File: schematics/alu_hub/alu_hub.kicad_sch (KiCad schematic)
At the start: 39 parts, among them U1 74LS574, U10 74LS02, U2 74LS245, U3 74LS02, U4 74LS181, U5 74LS181, U6 74LS574, U7 74LS245, U8 74LS245, U9 74LS02

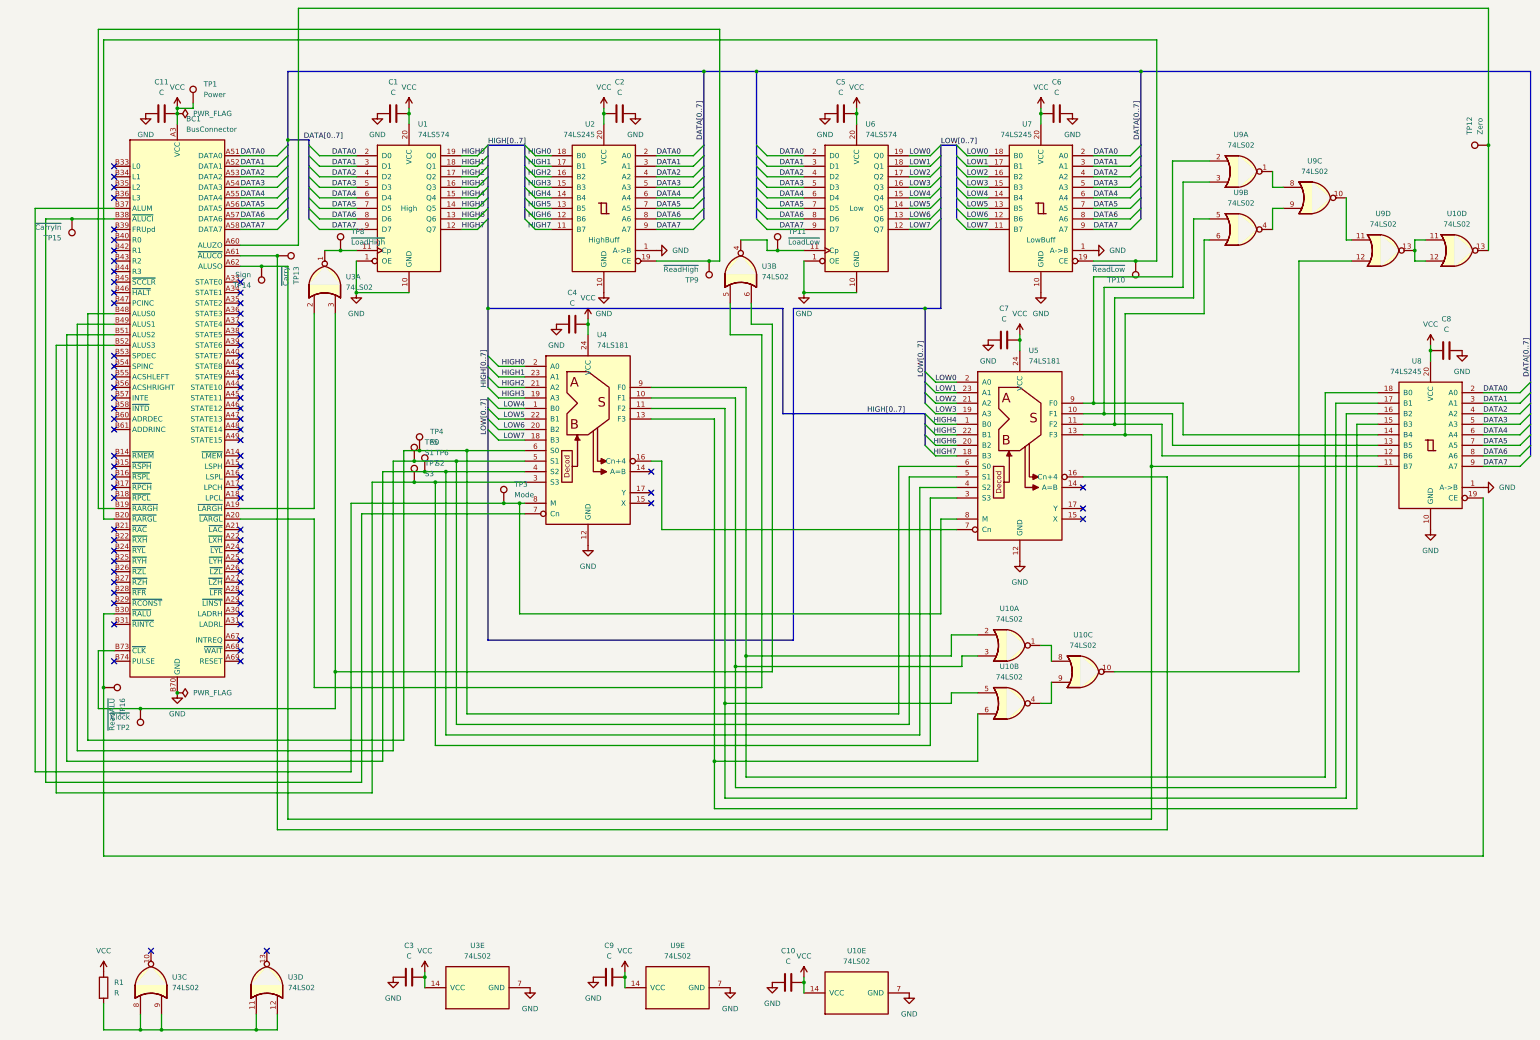
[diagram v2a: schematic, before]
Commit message: feat(alu): added tp to alu
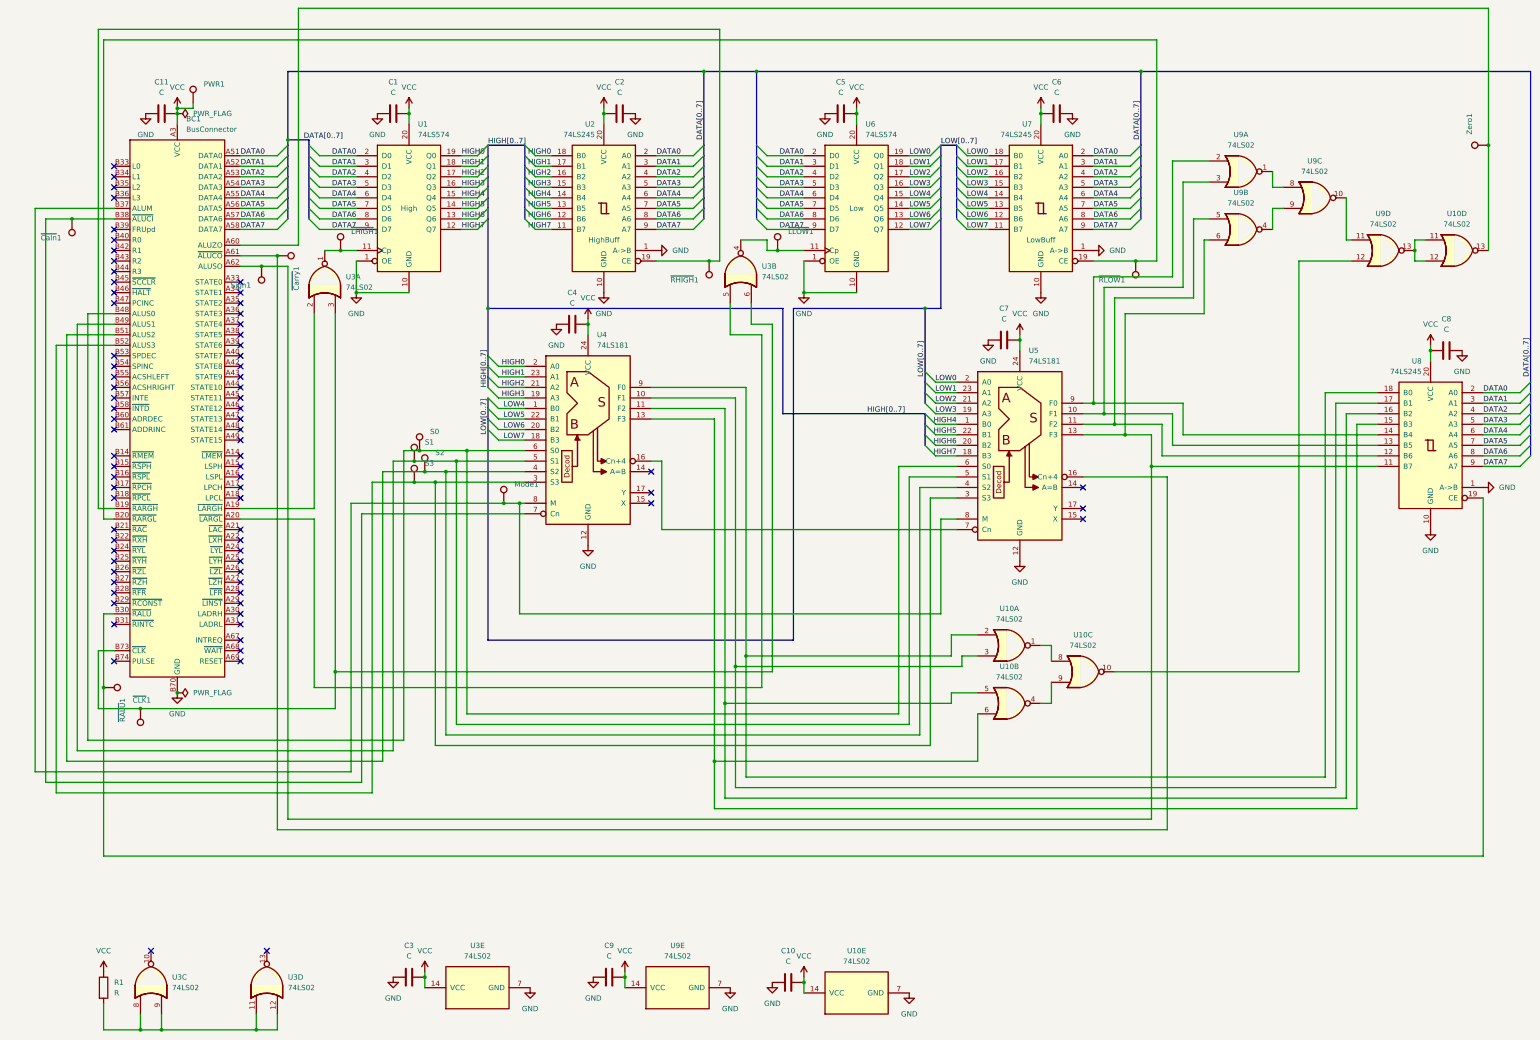
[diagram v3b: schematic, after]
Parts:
- Mode1: renamed from TP3; footprint Connector_Pin:Pin_D1.0mm_L10.0mm -> TestPoint:TestPoint_Pad_D1.0mm
- PWR1: renamed from TP1; footprint Connector_Pin:Pin_D1.0mm_L10.0mm -> TestPoint:TestPoint_Pad_D1.0mm
- S0: renamed from TP4; footprint Connector_Pin:Pin_D1.0mm_L10.0mm -> TestPoint:TestPoint_Pad_D1.0mm
- S1: renamed from TP5; footprint Connector_Pin:Pin_D1.0mm_L10.0mm -> TestPoint:TestPoint_Pad_D1.0mm
- S2: renamed from TP6; footprint Connector_Pin:Pin_D1.0mm_L10.0mm -> TestPoint:TestPoint_Pad_D1.0mm
- S3: renamed from TP7; footprint Connector_Pin:Pin_D1.0mm_L10.0mm -> TestPoint:TestPoint_Pad_D1.0mm
- Sign1: renamed from TP14; footprint Connector_Pin:Pin_D1.0mm_L10.0mm -> TestPoint:TestPoint_Pad_D1.0mm
- Zero1: renamed from TP12; footprint Connector_Pin:Pin_D1.0mm_L10.0mm -> TestPoint:TestPoint_Pad_D1.0mm
- ~{CLK}1: renamed from TP2; footprint Connector_Pin:Pin_D1.0mm_L10.0mm -> TestPoint:TestPoint_Pad_D1.0mm
- ~{CaIn}1: renamed from TP15; value ~{CarryIn} -> ~{CaIn}; footprint Connector_Pin:Pin_D1.0mm_L10.0mm -> TestPoint:TestPoint_Pad_D1.0mm
- ~{Carry}1: renamed from TP13; footprint Connector_Pin:Pin_D1.0mm_L10.0mm -> TestPoint:TestPoint_Pad_D1.0mm
- ~{LHIGH}1: renamed from TP8; footprint Connector_Pin:Pin_D1.0mm_L10.0mm -> TestPoint:TestPoint_Pad_D1.0mm
- ~{LLOW}1: renamed from TP11; footprint Connector_Pin:Pin_D1.0mm_L10.0mm -> TestPoint:TestPoint_Pad_D1.0mm
- ~{RALU}1: renamed from TP16; footprint Connector_Pin:Pin_D1.0mm_L10.0mm -> TestPoint:TestPoint_Pad_D1.0mm
- ~{RHIGH}1: renamed from TP9; footprint Connector_Pin:Pin_D1.0mm_L10.0mm -> TestPoint:TestPoint_Pad_D1.0mm
- ~{RLOW}1: renamed from TP10; footprint Connector_Pin:Pin_D1.0mm_L10.0mm -> TestPoint:TestPoint_Pad_D1.0mm
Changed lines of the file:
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@@
 		(on_board yes)
 		(dnp no)
-		(property "Reference" "TP10"
+		(property "Reference" "~{RLOW}1"
 			(at 288.29 93.4721 0)
 			(effects
@@
 				)
 				(justify left)
+				(hide yes)
 			)
 		)
-		(property "Footprint" "Connector_Pin:Pin_D1.0mm_L10.0mm"
+		(property "Footprint" "TestPoint:TestPoint_Pad_D1.0mm"
 			(at 285.75 88.9 0)
 			(effects
@@
 			(project "alu_hub"
 				(path "/63bf5833-673b-41a8-8365-6351cd154882"
-					(reference "TP10")
+					(reference "~{RLOW}1")
 					(unit 1)
 				)
@@
 		(on_board yes)
 		(dnp no)
-		(property "Reference" "TP15"
+		(property "Reference" "~{CaIn}1"
 			(at 31.75 83.3121 0)
 			(effects
@@
 			)
 		)
-		(property "Value" "~{CarryIn}"
+		(property "Value" "~{CaIn}"
 			(at 31.75 80.7721 0)
 			(effects
@@
 				)
 				(justify left)
+				(hide yes)
 			)
 		)
-		(property "Footprint" "Connector_Pin:Pin_D1.0mm_L10.0mm"
+		(property "Footprint" "TestPoint:TestPoint_Pad_D1.0mm"
 			(at 29.21 78.74 0)
 			(effects
@@
 			(project "alu_hub"
 				(path "/63bf5833-673b-41a8-8365-6351cd154882"
-					(reference "TP15")
+					(reference "~{CaIn}1")
 					(unit 1)
 				)
@@
 		(on_board yes)
 		(dnp no)
-		(property "Reference" "TP12"
+		(property "Reference" "Zero1"
 			(at 371.3479 58.42 0)
 			(effects
@@
 				)
 				(justify left)
+				(hide yes)
 			)
 		)
-		(property "Footprint" "Connector_Pin:Pin_D1.0mm_L10.0mm"
+		(property "Footprint" "TestPoint:TestPoint_Pad_D1.0mm"
 			(at 375.92 55.88 0)
 			(effects
@@
 			(project "alu_hub"
 				(path "/63bf5833-673b-41a8-8365-6351cd154882"
-					(reference "TP12")
+					(reference "Zero1")
 					(unit 1)
 				)
@@
 		(on_board yes)
 		(dnp no)
-		(property "Reference" "TP14"
+		(property "Reference" "Sign1"
 			(at 77.47 94.7421 0)
 			(effects
@@
 				)
 				(justify left)
+				(hide yes)
 			)
 		)
-		(property "Footprint" "Connector_Pin:Pin_D1.0mm_L10.0mm"
+		(property "Footprint" "TestPoint:TestPoint_Pad_D1.0mm"
 			(at 74.93 90.17 0)
 			(effects
@@
 			(project "alu_hub"
 				(path "/63bf5833-673b-41a8-8365-6351cd154882"
-					(reference "TP14")
+					(reference "Sign1")
 					(unit 1)
 				)
@@
 		(on_board yes)
 		(dnp no)
-		(property "Reference" "TP11"
+		(property "Reference" "~{LLOW}1"
 			(at 207.01 81.7879 0)
 			(effects
@@
 				)
 				(justify left)
+				(hide yes)
 			)
 		)
-		(property "Footprint" "Connector_Pin:Pin_D1.0mm_L10.0mm"
+		(property "Footprint" "TestPoint:TestPoint_Pad_D1.0mm"
 			(at 209.55 86.36 0)
 			(effects
@@
 			(project "alu_hub"
 				(path "/63bf5833-673b-41a8-8365-6351cd154882"
-					(reference "TP11")
+					(reference "~{LLOW}1")
 					(unit 1)
 				)
@@
 		(on_board yes)
 		(dnp no)
-		(property "Reference" "TP1"
+		(property "Reference" "PWR1"
 			(at 66.04 46.2279 0)
 			(effects
@@
 				)
 				(justify left)
+				(hide yes)
 			)
 		)
-		(property "Footprint" "Connector_Pin:Pin_D1.0mm_L10.0mm"
+		(property "Footprint" "TestPoint:TestPoint_Pad_D1.0mm"
 			(at 68.58 50.8 0)
 			(effects
@@
 			(project "alu_hub"
 				(path "/63bf5833-673b-41a8-8365-6351cd154882"
-					(reference "TP1")
+					(reference "PWR1")
 					(unit 1)
 				)
@@
 		(on_board yes)
 		(dnp no)
-		(property "Reference" "TP13"
+		(property "Reference" "~{Carry}1"
 			(at 88.3921 90.17 0)
 			(effects
@@
 				)
 				(justify left)
+				(hide yes)
 			)
 		)
-		(property "Footprint" "Connector_Pin:Pin_D1.0mm_L10.0mm"
+		(property "Footprint" "TestPoint:TestPoint_Pad_D1.0mm"
 			(at 83.82 92.71 0)
 			(effects
@@
 			(project "alu_hub"
 				(path "/63bf5833-673b-41a8-8365-6351cd154882"
-					(reference "TP13")
+					(reference "~{Carry}1")
 					(unit 1)
 				)
@@
 		(on_board yes)
 		(dnp no)
-		(property "Reference" "TP16"
+		(property "Reference" "~{RALU}1"
 			(at 46.4821 194.31 0)
 			(effects
@@
 				)
 				(justify left)
+				(hide yes)
 			)
 		)
-		(property "Footprint" "Connector_Pin:Pin_D1.0mm_L10.0mm"
+		(property "Footprint" "TestPoint:TestPoint_Pad_D1.0mm"
 			(at 41.91 196.85 0)
 			(effects
@@
 			(project "alu_hub"
 				(path "/63bf5833-673b-41a8-8365-6351cd154882"
-					(reference "TP16")
+					(reference "~{RALU}1")
 					(unit 1)
 				)
@@
 		(on_board yes)
 		(dnp no)
-		(property "Reference" "TP9"
+		(property "Reference" "~{RHIGH}1"
 			(at 185.42 93.4721 0)
 			(effects
@@
 				)
 				(justify left)
+				(hide yes)
 			)
 		)
-		(property "Footprint" "Connector_Pin:Pin_D1.0mm_L10.0mm"
+		(property "Footprint" "TestPoint:TestPoint_Pad_D1.0mm"
 			(at 182.88 88.9 0)
 			(effects
@@
 			(project "alu_hub"
 				(path "/63bf5833-673b-41a8-8365-6351cd154882"
-					(reference "TP9")
+					(reference "~{RHIGH}1")
 					(unit 1)
 				)
@@
 		(on_board yes)
 		(dnp no)
-		(property "Reference" "TP8"
+		(property "Reference" "~{LHIGH}1"
 			(at 101.6 81.7879 0)
 			(effects
@@
 				)
 				(justify left)
+				(hide yes)
 			)
 		)
-		(property "Footprint" "Connector_Pin:Pin_D1.0mm_L10.0mm"
+		(property "Footprint" "TestPoint:TestPoint_Pad_D1.0mm"
 			(at 104.14 86.36 0)
 			(effects
@@
 			(project "alu_hub"
 				(path "/63bf5833-673b-41a8-8365-6351cd154882"
-					(reference "TP8")
+					(reference "~{LHIGH}1")
 					(unit 1)
 				)
@@
 		(on_board yes)
 		(dnp no)
-		(property "Reference" "TP4"
+		(property "Reference" "S0"
 			(at 120.65 130.0479 0)
 			(effects
@@
 				)
 				(justify left)
+				(hide yes)
 			)
 		)
-		(property "Footprint" "Connector_Pin:Pin_D1.0mm_L10.0mm"
+		(property "Footprint" "TestPoint:TestPoint_Pad_D1.0mm"
 			(at 123.19 134.62 0)
 			(effects
@@
 			(project "alu_hub"
 				(path "/63bf5833-673b-41a8-8365-6351cd154882"
-					(reference "TP4")
+					(reference "S0")
 					(unit 1)
 				)
@@
 		(on_board yes)
 		(dnp no)
-		(property "Reference" "TP7"
+		(property "Reference" "S3"
 			(at 119.38 137.6679 0)
 			(effects
@@
 				)
 				(justify left)
+				(hide yes)
 			)
 		)
-		(property "Footprint" "Connector_Pin:Pin_D1.0mm_L10.0mm"
+		(property "Footprint" "TestPoint:TestPoint_Pad_D1.0mm"
 			(at 121.92 142.24 0)
 			(effects
@@
 			(project "alu_hub"
 				(path "/63bf5833-673b-41a8-8365-6351cd154882"
-					(reference "TP7")
+					(reference "S3")
 					(unit 1)
 				)
@@
 		(on_board yes)
 		(dnp no)
-		(property "Reference" "TP5"
+		(property "Reference" "S1"
 			(at 119.38 132.5879 0)
 			(effects
@@
 				)
 				(justify left)
+				(hide yes)
 			)
 		)
-		(property "Footprint" "Connector_Pin:Pin_D1.0mm_L10.0mm"
+		(property "Footprint" "TestPoint:TestPoint_Pad_D1.0mm"
 			(at 121.92 137.16 0)
 			(effects
@@
 			(project "alu_hub"
 				(path "/63bf5833-673b-41a8-8365-6351cd154882"
-					(reference "TP5")
+					(reference "S1")
 					(unit 1)
 				)
@@
 		(on_board yes)
 		(dnp no)
-		(property "Reference" "TP2"
-			(at 48.26 201.4221 0)
+		(property "Reference" "~{CLK}1"
+			(at 53.34 194.818 0)
 			(effects
 				(font
@@
 		)
 		(property "Value" "~{Clock}"
-			(at 48.26 198.8821 0)
+			(at 53.34 192.278 0)
 			(effects
 				(font
@@
 				)
 				(justify left)
+				(hide yes)
 			)
 		)
-		(property "Footprint" "Connector_Pin:Pin_D1.0mm_L10.0mm"
+		(property "Footprint" "TestPoint:TestPoint_Pad_D1.0mm"
 			(at 45.72 196.85 0)
 			(effects
@@
 			(project "alu_hub"
 				(path "/63bf5833-673b-41a8-8365-6351cd154882"
-					(reference "TP2")
+					(reference "~{CLK}1")
 					(unit 1)
 				)
@@
 		(on_board yes)
 		(dnp no)
-		(property "Reference" "TP3"
+		(property "Reference" "Mode1"
 			(at 140.97 142.7479 0)
 			(effects
@@
 				)
 				(justify left)
+				(hide yes)
 			)
 		)
-		(property "Footprint" "Connector_Pin:Pin_D1.0mm_L10.0mm"
+		(property "Footprint" "TestPoint:TestPoint_Pad_D1.0mm"
 			(at 143.51 147.32 0)
 			(effects
@@
 			(project "alu_hub"
 				(path "/63bf5833-673b-41a8-8365-6351cd154882"
-					(reference "TP3")
+					(reference "Mode1")
 					(unit 1)
 				)
@@
 		(on_board yes)
 		(dnp no)
-		(property "Reference" "TP6"
+		(property "Reference" "S2"
 			(at 121.92 135.1279 0)
 			(effects
@@
 				)
 				(justify left)
+				(hide yes)
 			)
 		)
-		(property "Footprint" "Connector_Pin:Pin_D1.0mm_L10.0mm"
+		(property "Footprint" "TestPoint:TestPoint_Pad_D1.0mm"
 			(at 124.46 139.7 0)
 			(effects
@@
 			(project "alu_hub"
 				(path "/63bf5833-673b-41a8-8365-6351cd154882"
-					(reference "TP6")
+					(reference "S2")
 					(unit 1)
 				)

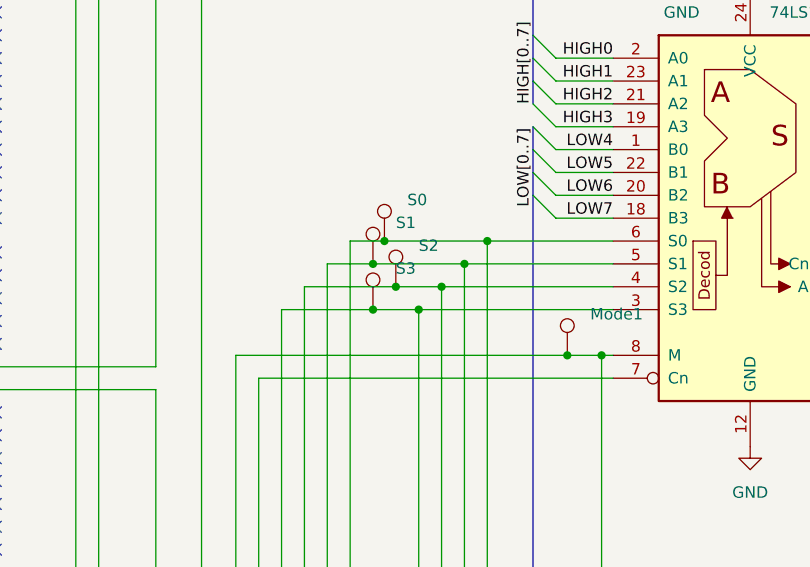
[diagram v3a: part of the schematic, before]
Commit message: fix(alu, interface): fix tp
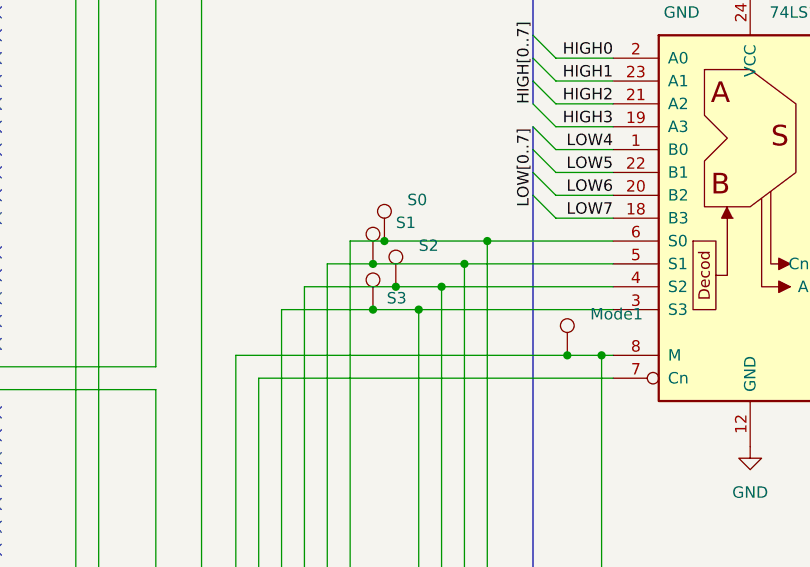
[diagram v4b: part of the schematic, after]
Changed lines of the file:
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@@
 		(dnp no)
 		(property "Reference" "S3"
-			(at 119.38 137.6679 0)
+			(at 118.364 140.97 0)
 			(effects
 				(font
